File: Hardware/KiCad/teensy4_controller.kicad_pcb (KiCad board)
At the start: 4 copper layers, 100 x 65 mm, 90 parts, among them J1 Screw_Terminal_01x04, J10 Conn_01x04, J11 Conn_01x03, J12 Conn_01x03, J13 Conn_01x03, J14 Conn_01x03, J15 Conn_01x02, J16 Conn_02x04_Odd_Even, J17 Conn_01x04, J18 Conn_01x04, J19 Conn_01x02, J2 Conn_01x05, J20 Screw_Terminal_01x02, J21 Screw_Terminal_01x02, J22 Conn_02x04_Odd_Even, J23 Conn_01x04, J24 Screw_Terminal_01x02, J25 Screw_Terminal_01x02, J26 Screw_Terminal_01x02, J27 Screw_Terminal_01x02, J28 Screw_Terminal_01x02, J29 Screw_Terminal_01x02, J3 Conn_01x05, J30 Screw_Terminal_01x02, J31 RJ45_Wiznet_RB1-125BAG1A, J4 Conn_01x05, J5 Conn_01x04, J6 Conn_01x04, J7 Conn_01x03, J8 Conn_01x02, J9 Conn_02x04_Odd_Even, U1 74LVC3G06, U2 74LVC3G06, U3 74LVC3G06, U4 MPXA6115A, U5 MPXA6115A, U6 Teensy4.1, U7 R-78E5.0-1.0, U8 ULN2003AD

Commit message: Update
As ordered
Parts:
- C1: value CP1 -> 47uF
- C5: footprint Resistor_SMD:R_0603_1608Metric_Pad1.05x0.95mm_HandSolder -> Capacitor_SMD:C_0603_1608Metric_Pad1.05x0.95mm_HandSolder
- J1: footprint TerminalBlock_Phoenix:TerminalBlock_Phoenix_MKDS-1,5-4-5.08_1x04_P5.08mm_Horizontal -> TerminalBlock_Phoenix:TerminalBlock_Phoenix_MKDS-1,5-4_1x04_P5.00mm_Horizontal
- U1, U2, U3: value 74LVC3G06 -> 74LVC3G07
- moved FID2 26.2 mm to (110.5, 91.4)
- moved R8 21.2 mm to (96.0, 113.6)
- moved FID3 18.5 mm to (60.3, 88.9)
- moved FID1 1.55 mm to (78.7, 146.9)
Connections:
- net /MOT_X_CS renamed /MOT_A_CS
- net /MOT_Y_CS renamed /MOT_B_CS
- net /MOT_Z_CS renamed /MOT_C_CS
- net /X_CS renamed /A_CS
- net /X_M1 renamed /A_M1
- net /X_M2 renamed /A_M2
- net /X_M3 renamed /A_M3
- net /X_RST renamed /A_RST
- net /X_SLP renamed /A_SLP
- net /Y_CS renamed /B_CS
- net /Y_M1 renamed /B_M1
- net /Y_M2 renamed /B_M2
- net /Y_M3 renamed /B_M3
- net /Y_RST renamed /B_RST
- net /Y_SLP renamed /B_SLP
- net /Z_CS renamed /C_CS
- net /Z_M1 renamed /C_M1
- net /Z_M2 renamed /C_M2
- net /Z_M3 renamed /C_M3
- net /Z_RST renamed /C_RST
- net /Z_SLP renamed /C_SLP
- A1 pad 15: /X_STEP -> /A_STEP
- A1 pad 16: /X_DIR -> /A_DIR
- A1 pad 9: /X_ENABLE -> /A_ENABLE
- A2 pad 15: /Y_STEP -> /B_STEP
- A2 pad 16: /Y_DIR -> /B_DIR
- A2 pad 9: /Y_ENABLE -> /B_ENABLE
- A3 pad 15: /Z_STEP -> /C_STEP
- A3 pad 16: /Z_DIR -> /C_DIR
- A3 pad 9: /Z_ENABLE -> /C_ENABLE
- U6 pad 10: /Y_DIR -> /B_DIR
- U6 pad 11: /Y_STEP -> /B_STEP
- U6 pad 12: Net-(U6-Pad12) -> /Y_DIR
- U6 pad 16: Net-(U6-Pad16) -> /Y_STEP
- U6 pad 17: /Y_ENABLE -> /B_ENABLE
- U6 pad 19: /Z_DIR -> /C_DIR
- U6 pad 20: /Z_STEP -> /C_STEP
- U6 pad 21: Net-(U6-Pad21) -> /Z_DIR
- U6 pad 22: Net-(U6-Pad22) -> /Z_STEP
- U6 pad 23: /Z_ENABLE -> /C_ENABLE
- U6 pad 3: /X_DIR -> /A_DIR
- U6 pad 4: /X_STEP -> /A_STEP
- U6 pad 44: Net-(U6-Pad44) -> /Z_ENABLE
- U6 pad 45: Net-(U6-Pad45) -> /Y_ENABLE
- U6 pad 5: Net-(U6-Pad5) -> /X_DIR
- U6 pad 6: Net-(U6-Pad6) -> /X_STEP
- U6 pad 7: /X_ENABLE -> /A_ENABLE
- U6 pad 8: Net-(U6-Pad8) -> /X_ENABLE
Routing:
- net /Z_ENABLE: track 26.1 -> 84.5 mm
- net /Y_ENABLE: track 26.1 -> 81.6 mm, vias 0 -> 1
- net +24V: track 42.6 -> 67.3 mm
- net /SCK: track 19.7 -> 2.79 mm
- net /MOT_SCK: track 67.9 -> 82.8 mm
- net /Y_STEP: track 39.9 -> 28.0 mm
- net /X_DIR: track 41.6 -> 32.4 mm
- net /A_DIR: track 0.00 -> 8.45 mm
- net /X_STEP: track 37.2 -> 29.1 mm
- net /Z_STEP: track 37.3 -> 29.3 mm
- net /A_STEP: track 0.00 -> 7.82 mm
- net /C_STEP: track 0.00 -> 7.29 mm
- net /C_ENABLE: track 0.00 -> 7.29 mm
- net /C_DIR: track 0.00 -> 7.29 mm
- net /Z_DIR: track 41.2 -> 34.2 mm
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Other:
- board text added: "A"
- board text added: "B"
- board text added: "C"

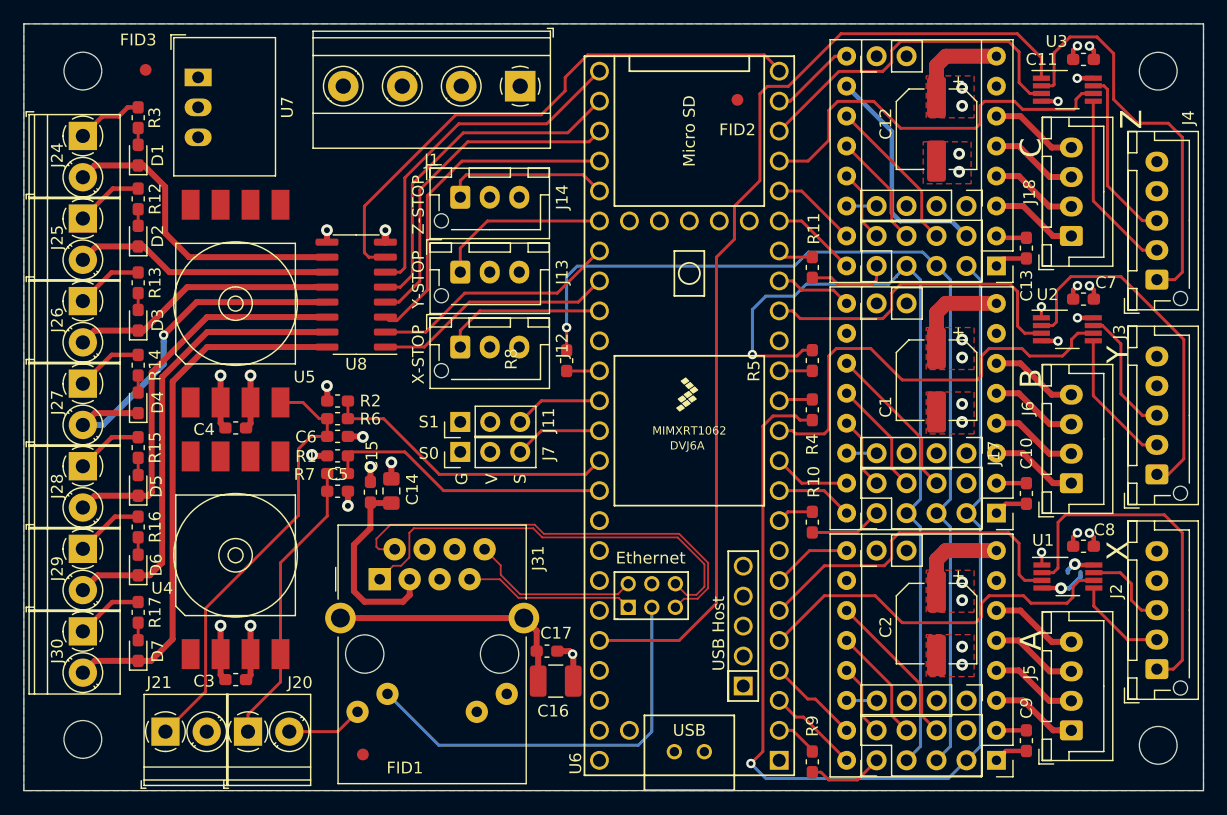
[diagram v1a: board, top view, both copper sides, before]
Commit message: Correct error on TMC SPI connections
MISO and CS were swapped at config jumpers
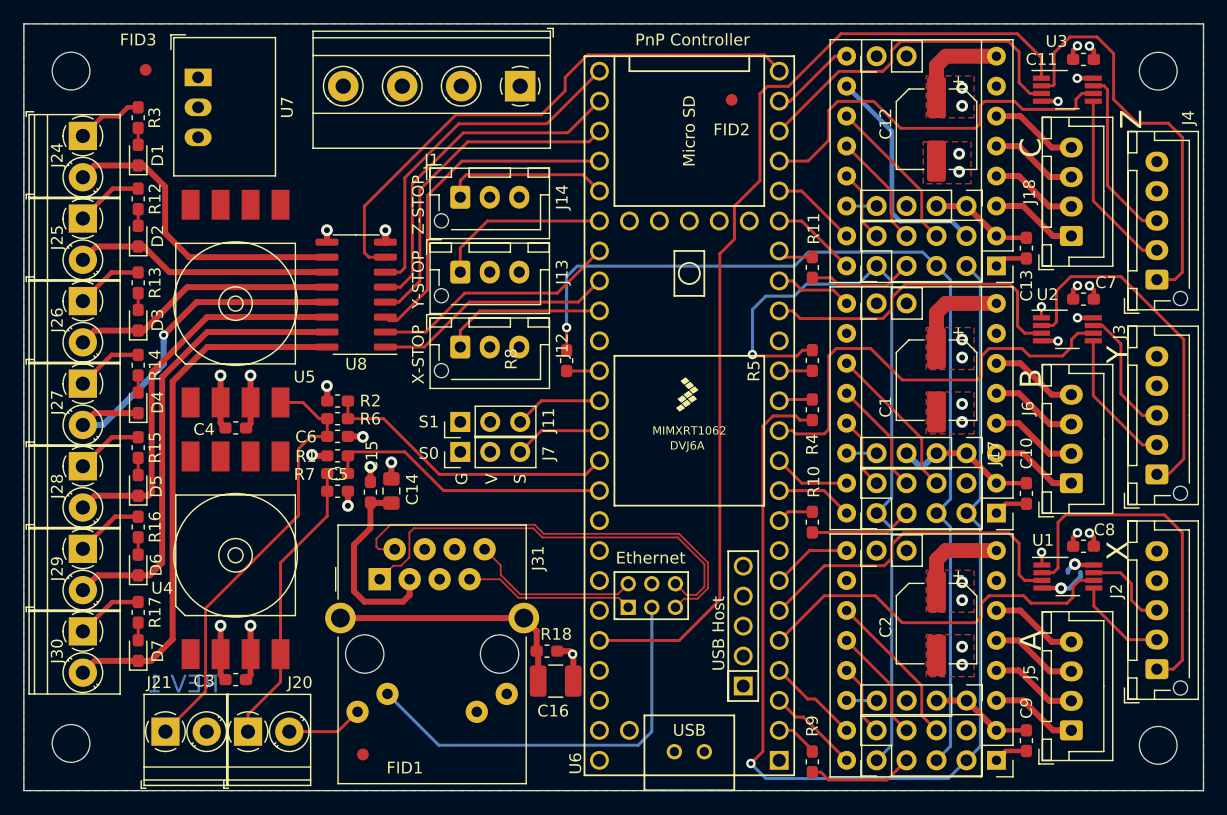
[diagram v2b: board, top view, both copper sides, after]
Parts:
- removed C17: 0.1uF, Capacitor_SMD:C_0603_1608Metric_Pad1.05x0.95mm_HandSolder
- added R18: 1M, Resistor_SMD:R_0603_1608Metric_Pad1.05x0.95mm_HandSolder, F.Cu at (94.3, 138.2)
- C16: value 1uF -> 1000pF
- U4, U5: value MPXA6115A -> MPXA6115V
- moved H1 1.06 mm to (54.0, 146.0)
- moved H2 1.00 mm to (54.0, 89.0)
- moved FID2 0.49 mm to (110.0, 91.4)
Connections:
- J16 pad 1: /MOT_B_CS -> /MOT_MISO
- J16 pad 3: /MOT_MISO -> /MOT_B_CS
- J22 pad 1: /MOT_C_CS -> /MOT_MISO
- J22 pad 3: /MOT_MISO -> /MOT_C_CS
- J9 pad 1: /MOT_A_CS -> /MOT_MISO
- J9 pad 3: /MOT_MISO -> /MOT_A_CS
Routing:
- net +5V: track 41.5 -> 53.2 mm
- net /MOT_B_CS: track 6.13 -> 8.67 mm
- net /MOT_A_CS: track 6.43 -> 8.95 mm
- net /MOT_MISO: track 67.6 -> 65.3 mm
- net /MOT_C_CS: track 7.10 -> 8.95 mm
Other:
- board text added: "PnP Controller"
- board text added: "REV 1"
